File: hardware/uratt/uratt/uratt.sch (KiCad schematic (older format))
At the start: 62 parts

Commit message: more schematic work.. power supply, lip charger, etc
more schematic work.. power supply, lip charger, etc
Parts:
- added C? (x2): .1uF, symbol Device:C_Small
- added C?: 1uF, symbol Device:C_Small
- added C? (x2): 2.2uF, symbol Device:C_Small
- added C? (x2): 4.7uF, symbol Device:C_Small
- added C?: 220uF, symbol Device:CP1_Small
- added C?: 10uF, symbol Device:C_Small
- added D?: LED, symbol Device:LED
- added J?: Conn_01x02, symbol Connector_Generic:Conn_01x02
- added L?: 6.8uH, symbol Device:L
- added R? (x5): 10K, symbol Device:R_Small_US
- added R? (x2): 1K, symbol Device:R_Small_US
- added R?: 270, symbol Device:R_Small_US
- added R?: 2K, symbol Device:R_Small_US
- added R?: 0, symbol Device:R_Small_US
- added R?: R3, symbol Device:R_Small_US
- added R?: R4, symbol Device:R_Small_US
- added R?: R1, symbol Device:R_Small_US
- added R?: R2, symbol Device:R_Small_US
- added U?: MCP73832-2-OT, Package_TO_SOT_SMD:SOT-23-5, symbol Battery_Management:MCP73832-2-OT
- added U?: TPS2115A, symbol uratt:TPS2115A
- added U?: TPS61032PWP, symbol uratt:TPS6103x
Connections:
- net labels added: +5VIN, +VBATT, +VSW, 5V_ENABLE, CHARGE_STATUS, GNDPWR, LOW_BAT, N_PWR_LOSS, SHUTDOWN
- wire segments 236 -> 376
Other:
- note added: "Charge Current Resistor\nI_CHG = 1000 / R_PROG\nR_PROG = 2K : I_CHG = 500mA"
- note added: "D1=0, D0=0, IN2>IN1=X, STAT=HI-Z, OUT=IN2\nD1=0, D0=1, IN2>IN1=N, STAT=0, OUT=IN1\nD1=0, D0=1, IN2>IN1=Y, STAT=HI-Z, OUT=IN2\nD1=1, D0=0, IN2>IN1=X, STAT=0, OUT=IN1\nD1=1, D0=1, IN2>IN1=X, STAT=0, OUT=HI-Z\n\n\n"
- note added: "R_PROG\n"
- moved on the sheet: C?, D?, FB?, J?, R?, U?

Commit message: mostly feature complete schematic?
Split off pages for power and front panel, assign all I/O, add alarm & exp, add 10V option off 5V boost for optional stepper driver (for cabinet lock-bot), ESD protection
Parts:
- removed C?: 10uF, symbol Device:CP1_Small
- removed C? (x2): 0.1uF, symbol Device:C_Small
- removed C? (x2): 1uF, symbol Device:C_Small
- removed C? (x2): .1uF, symbol Device:C_Small
- removed C? (x2): 2.2uF, symbol Device:C_Small
- removed C? (x2): 4.7uF, symbol Device:C_Small
- removed C?: 220uF, symbol Device:CP1_Small
- removed C?: 10uF, symbol Device:C_Small
- removed D?: LED, symbol Device:LED
- removed J? (x2): Conn_01x02, symbol Connector_Generic:Conn_01x02
- removed L?: 6.8uH, symbol Device:L
- removed Q?: DMP31D0U, Package_TO_SOT_SMD:SOT-23, symbol Transistor_FET:BSS83P
- removed R?: 220, symbol Device:R_Small_US
- removed R? (x6): 10K, symbol Device:R_Small_US
- removed R? (x2): 1K, symbol Device:R_Small_US
- removed R?: 270, symbol Device:R_Small_US
- removed R?: 2K, symbol Device:R_Small_US
- removed R?: 0, symbol Device:R_Small_US
- removed R?: R3, symbol Device:R_Small_US
- removed R?: R4, symbol Device:R_Small_US
- removed R?: R1, symbol Device:R_Small_US
- removed R?: R2, symbol Device:R_Small_US
- removed U?: MP6513, Package_TO_SOT_SMD:TSOT-23-6, symbol uratt:MP6513
- removed U?: ER-TFT0.96-1, symbol uratt:ER-TFT0.96-1
- removed U?: AP2112K-3.3, Package_TO_SOT_SMD:SOT-23-5, symbol Regulator_Linear:AP2112K-3.3
- removed U?: MCP73832-2-OT, Package_TO_SOT_SMD:SOT-23-5, symbol Battery_Management:MCP73832-2-OT
- removed U?: TPS2115A, symbol uratt:TPS2115A
- removed U?: TPS61032PWP, symbol uratt:TPS6103x
- added C? (x2): .1uF, symbol Device:C_Small
- added C? (x2): 2.2uF, symbol Device:C_Small
- added D?: DT1240A-08LP3810, Package_DFN_QFN:UDFN-9_1.0x3.8mm_P0.5mm, symbol Power_Protection:DT1240A-08LP3810
- added D? (x2): BAT54S, Package_TO_SOT_SMD:SOT-23, symbol Diode:BAT54S
- added J?: Conn_01x10, symbol Connector_Generic:Conn_01x10
- added J?: Conn_01x04, symbol Connector_Generic:Conn_01x04
- added R? (x5): 47, symbol Device:R_Small_US
- C?: value 100uF/6.3V -> 100uF
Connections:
- net labels added: +3.3VSW, +5VSW, +5VUSB, ALARM_SW, EXP, FP_TOUCH_BTN, PWR_ENABLE
- net labels removed: +5V, +5VIN, +5VP, +VBATT, +VSW, 5V_ENABLE, 5V_RFID_TX, CHARGE_STATUS, GNDPWR, RFID_RX, RFID_TX
- wire segments 376 -> 273
- no-connect marks 13 -> 20
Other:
- note added: "ALARM & EXP I/O"
- note added: "FRONT PANEL CONNECTOR"
- note added: "POPULATE ONLY ONE\n5V is FB?\n3.3V is FB?"
- note removed: "BACKLIGHT\nVF=3.2V IF=15mA\n"
- note removed: "Charge Current Resistor\nI_CHG = 1000 / R_PROG\nR_PROG = 2K : I_CHG = 500mA"
- note removed: "D1=0, D0=0, IN2>IN1=X, STAT=HI-Z, OUT=IN2\nD1=0, D0=1, IN2>IN1=N, STAT=0, OUT=IN1\nD1=0, D0=1, IN2>IN1=Y, STAT=HI-Z, OUT=IN2\nD1=1, D0=0, IN2>IN1=X, STAT=0, OUT=IN1\nD1=1, D0=1, IN2>IN1=X, STAT=0, OUT=HI-Z\n\n\n"
- note removed: "DC MOTOR CONTROL"
- note removed: "GRAPHIC LCD"
- note removed: "POPULATE ONLY ONE\n5V is R?\n3.3V is R?"
- note removed: "RFID_TX is the OUTPUT from the external RFID module (transmitted RFID tag data)\nRFID_RX is the INPUT to the external RFID module (optional command to RFID)"
- note removed: "R_PROG\n"
- moved on the sheet: BZ?, C?, D?, FB?, J?, Q?, R?, U?

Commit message: uRATT rough footprint assignment and placement for fitment
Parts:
- removed BZ?: Buzzer, symbol Device:Buzzer
- removed Q? (x2): S8050, Package_TO_SOT_THT:TO-92_Inline, symbol Transistor_BJT:S8050
- removed Q?: 2N7002, Package_TO_SOT_SMD:SOT-23, symbol Transistor_FET:2N7002
- removed R?: 100, symbol Device:R_Small_US
- removed R?: 1K, symbol Device:R_Small_US
- added Q1, Q2: MMBT3904, Package_TO_SOT_SMD:SOT-23, symbol Transistor_BJT:MMBT3904
- C1, C5: renamed from C?; footprint (none) -> Capacitor_SMD:C_0805_2012Metric
- C10, C11, C13, C14, C15, C16, C2, C3, C4, C6, C7, C8, C9: renamed from C?; footprint (none) -> Capacitor_SMD:C_0603_1608Metric
- C12: renamed from C?; footprint (none) -> Capacitor_SMD:CP_Elec_5x3
- D1: renamed from D?; footprint Diode_THT:D_DO-41_SOD81_P10.16mm_Horizontal -> Diode_SMD:D_0805_2012Metric
- FB1, FB2: renamed from FB?; footprint (none) -> Inductor_SMD:L_0603_1608Metric
- J1: renamed from J?; footprint (none) -> Connector_USB:USB_Micro-B_Molex-105133-0001
- J2: renamed from J?; footprint (none) -> Connector_Card:microSD_HC_Hirose_DM3D-SF
- J3: renamed from J?; footprint (none) -> Connector_PinHeader_2.54mm:PinHeader_1x10_P2.54mm_Vertical
- J4, J5: renamed from J?; footprint (none) -> Connector_JST:JST_PH_B4B-PH-K_1x04_P2.00mm_Vertical
- R1, R10, R11, R12, R13, R14, R15, R16, R17, R19, R2, R21, R22, R23, R24, R25, R26, R27, R3, R4, R5, R6, R7, R8, R9: renamed from R?; footprint (none) -> Resistor_SMD:R_0603_1608Metric
- SW1, SW2: renamed from SW?; footprint (none) -> Button_Switch_SMD:SW_Push_1P1T_NO_CK_KMR2
- gave numbers to parts that had none: 8
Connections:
- net BEEPER: now also D2.9 (K8), J3.8 (Pin_8)
- net DTR: now also Q2.2 (E)
- net EN: now also Q1.3 (C)
- net GND: no longer J3.8 (Pin_8)
- net IO0: now also Q2.3 (C)
- net RTS: now also Q1.2 (E)
- net at R12.1: now also Q1.1 (B)
- net at R13.1: now also Q2.1 (B)
- no-connect marks 20 -> 19
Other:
- note removed: "PIEZO BEEPER"

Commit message: import actual board outline DXF and adjust rough placement
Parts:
- J3: footprint Connector_PinHeader_2.54mm:PinHeader_1x10_P2.54mm_Vertical -> Connector_PinHeader_2.00mm:PinHeader_1x10_P2.00mm_Vertical
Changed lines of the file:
@@
 F 0 "J3" H 14300 2100 50  0000 C CNN
 F 1 "Conn_01x10" H 14450 950 50  0000 C CNN
-F 2 "Connector_PinHeader_2.54mm:PinHeader_1x10_P2.54mm_Vertical" H 14300 1600 50  0001 C CNN
+F 2 "Connector_PinHeader_2.00mm:PinHeader_1x10_P2.00mm_Vertical" H 14300 1600 50  0001 C CNN
 F 3 "~" H 14300 1600 50  0001 C CNN
 	1    14300 1600

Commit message: WIP routing
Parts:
- J1: footprint Connector_USB:USB_Micro-B_Molex-105133-0001 -> Connector_FFC-FPC:TE_1-1734839-0_1x10-1MP_P0.5mm_Horizontal
- J3: footprint Connector_PinHeader_2.00mm:PinHeader_1x10_P2.00mm_Vertical -> Connector_FFC-FPC:Hirose_FH12-10S-0.5SH_1x10-1MP_P0.50mm_Horizontal
- renumbered R19 to R18, R21 to R19, R22 to R20, R23 to R21, R24 to R22, R25 to R23, R26 to R24, R27 to R25
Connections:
- net +3.3VSW: now also C5.1, C6.1, U2.5 (VIO), U2.6 (VDD), U2.7 (REGIN)
- net +3V3: no longer C5.1, C6.1, U2.5 (VIO), U2.6 (VDD), U2.7 (REGIN)
- net BEEPER: now also D2.6 (K5); no longer D2.9 (K8)
- net FP_TOUCH_BTN: now also D2.5 (K4); no longer D2.8 (K7)
- net LCD_CLK: now also D2.7 (K6); no longer D2.6 (K5)
- net LCD_CS: now also D2.9 (K8); no longer D2.2 (K2)
- net LCD_DC: now also D2.8 (K7); no longer D2.5 (K4)
- net LCD_MOSI: now also D2.4 (K3); no longer D2.7 (K6)
- net LCD_RESET: now also D2.2 (K2); no longer D2.4 (K3)

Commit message: fully routed, DRC'd, outlined w/breakaways, pending final review
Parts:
- J1: footprint Connector_FFC-FPC:TE_1-1734839-0_1x10-1MP_P0.5mm_Horizontal -> Connector_USB:USB_Micro-B_Molex-105133-0001
- J3: footprint Connector_FFC-FPC:Hirose_FH12-10S-0.5SH_1x10-1MP_P0.50mm_Horizontal -> Connector_FFC-FPC:TE_1-1734839-0_1x10-1MP_P0.5mm_Horizontal
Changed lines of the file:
@@
 F 0 "J1" H 1357 2017 50  0000 C CNN
 F 1 "USB_B_Micro" H 1357 1926 50  0000 C CNN
-F 2 "Connector_FFC-FPC:TE_1-1734839-0_1x10-1MP_P0.5mm_Horizontal" H 1450 1500 50  0001 C CNN
+F 2 "Connector_USB:USB_Micro-B_Molex-105133-0001" H 1450 1500 50  0001 C CNN
 F 3 "~" H 1450 1500 50  0001 C CNN
 	1    1300 1550
@@
 F 0 "J3" H 14300 2100 50  0000 C CNN
 F 1 "Conn_01x10" H 14450 950 50  0000 C CNN
-F 2 "Connector_FFC-FPC:Hirose_FH12-10S-0.5SH_1x10-1MP_P0.50mm_Horizontal" H 14300 1600 50  0001 C CNN
+F 2 "Connector_FFC-FPC:TE_1-1734839-0_1x10-1MP_P0.5mm_Horizontal" H 14300 1600 50  0001 C CNN
 F 3 "~" H 14300 1600 50  0001 C CNN
 	1    14300 1600
@@
 Connection ~ 4450 1050
 $Comp
-L uratt:+3.3VSW #PWR?
+L uratt:+3.3VSW #PWR0102
 U 1 1 601AE667
 P 3950 2350
-F 0 "#PWR?" H 3950 2200 50  0001 C CNN
+F 0 "#PWR0102" H 3950 2200 50  0001 C CNN
 F 1 "+3.3VSW" H 3965 2523 50  0000 C CNN
 F 2 "" H 3950 2350 50  0001 C CNN

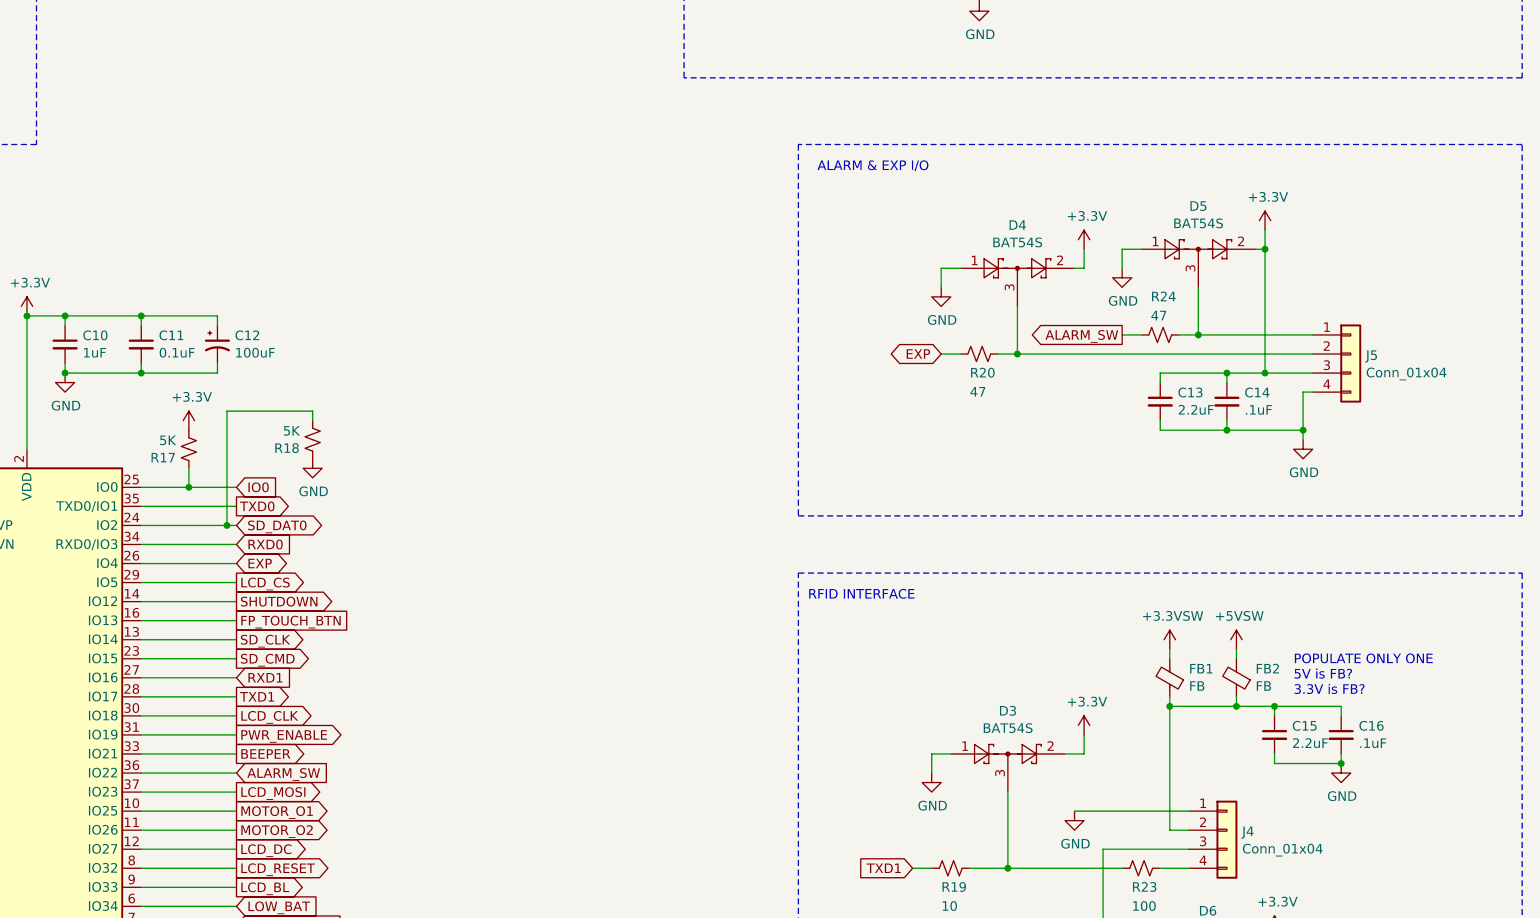
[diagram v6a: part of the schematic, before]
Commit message: add wire passthru slot, move & finalize flat flex, bigger fp button, 10V option for motor, exp connector now Grove with I2C option
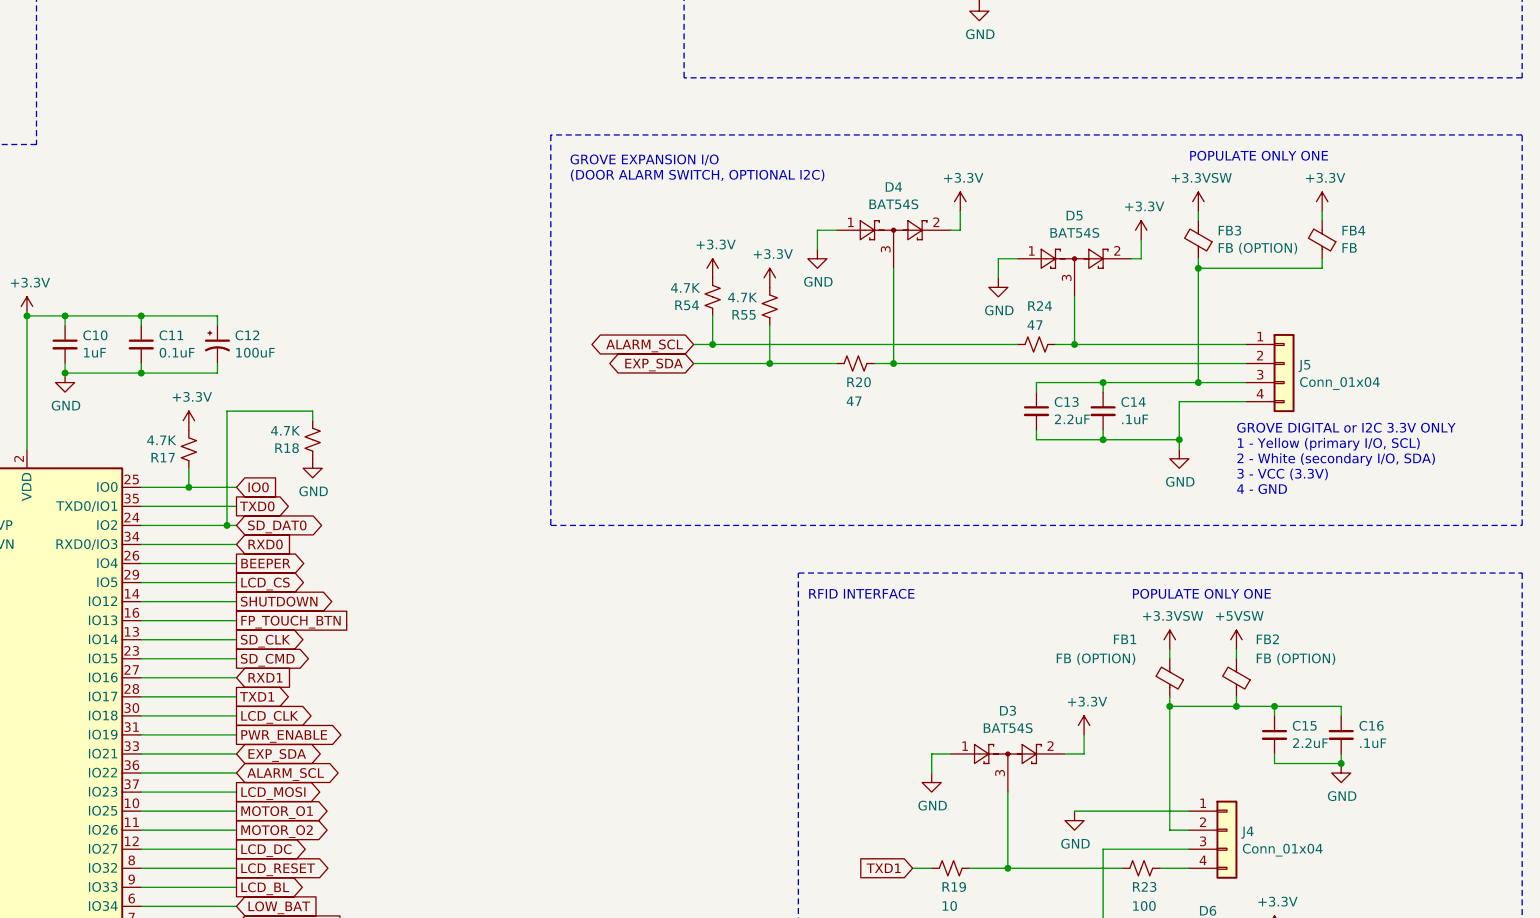
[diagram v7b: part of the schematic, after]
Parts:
- added FB3: FB (OPTION), Inductor_SMD:L_0603_1608Metric, symbol Device:Ferrite_Bead_Small
- added FB4: FB, Inductor_SMD:L_0603_1608Metric, symbol Device:Ferrite_Bead_Small
- added R54, R55: 4.7K, Resistor_SMD:R_0603_1608Metric, symbol Device:R_Small_US
- FB1, FB2: value FB -> FB (OPTION)
- J5: footprint Connector_JST:JST_PH_B4B-PH-K_1x04_P2.00mm_Vertical -> Connector:NS-Tech_Grove_1x04_P2mm_Vertical
- R17, R18: value 5K -> 4.7K
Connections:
- net +3.3VSW: now also FB3.2
- net +3V3: now also FB4.2, R54.2, R55.2; no longer C13.1, C14.1, J5.3 (Pin_3)
- net BEEPER: now also U3.26 (IO4); no longer U3.33 (IO21)
- net ALARM_SW renamed ALARM_SCL
- net ALARM_SCL: now also R54.1
- net EXP renamed EXP_SDA
- net EXP_SDA: now also U3.33 (IO21), R55.1; no longer U3.26 (IO4)
- new net: C13.1, C14.1, FB3.1, FB4.1, J5.3 (Pin_3)
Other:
- note added: "GROVE DIGITAL or I2C 3.3V ONLY\n1 - Yellow (primary I/O, SCL)\n2 - White (secondary I/O, SDA)\n3 - VCC (3.3V)\n4 - GND"
- note added: "GROVE EXPANSION I/O\n(DOOR ALARM SWITCH, OPTIONAL I2C)"
- note added: "POPULATE ONLY ONE"
- note removed: "ALARM & EXP I/O"
- note removed: "POPULATE ONLY ONE\n5V is FB?\n3.3V is FB?"
- moved on the sheet: C13, C14, D4, D5, J5, R20, R24

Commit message: completed BOM, 3D STEP export
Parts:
- C1, C5: Digikey (none) -> 1276-1096-1-ND
- C10, C3: Digikey (none) -> 587-2834-1-ND
- C11, C4: Digikey (none) -> 732-7939-1-ND
- C12: Digikey (none) -> PCE4156CT-ND
- C13, C15: Digikey (none) -> 1276-1085-1-ND
- C14, C16, C2, C6, C7, C8, C9: value .1uF -> 0.1uF; Digikey (none) -> 732-7939-1-ND
- D1: value 1N5819 -> SD0805S020S1R0; Digikey (none) -> 478-7800-1-ND
- D2: value DT1240A-08LP3810 -> DT1240A-08LP3810-7; Digikey (none) -> DT1240A-08LP3810-7DICT-ND
- D3, D4, D5, D6: Digikey (none) -> BAT54SLT1GOSCT-ND
- FB1, FB2, FB3: Digikey (none) -> 490-1012-1-ND
- FB4: value FB -> FB (OPTION); Digikey (none) -> 490-1012-1-ND
- J1: Digikey (none) -> WM9734CT-ND
- J2: Digikey (none) -> HR1941CT-ND
- J3: Alt MFR Part (none) -> ZF5S-10-01-T-WT-TR; Digikey (none) -> A100293CT-ND
- J4: Digikey (none) -> 455-1706-ND
- J5: Digikey (none) -> 1597-1082-ND
- Q1, Q2: Digikey (none) -> MMBT3904LT1GOSCT-ND
- R1, R2, R20, R24, R3: Digikey (none) -> 13-RT0603FRE0747RLCT-ND
- R10, R14, R15: Digikey (none) -> YAG5742CT-ND
- R11: Digikey (none) -> 2019-RK73Z1JTTDCT-ND
- R12, R13, R16: Digikey (none) -> YAG3353CT-ND
- R17, R18, R54, R55: Digikey (none) -> YAG1238CT-ND
- R19, R25: Digikey (none) -> 13-RE0603FRE0710RLCT-ND
- R21: Digikey (none) -> 13-RE0603FRE071KLCT-ND
- R22: Digikey (none) -> 13-RT0603FRE072K05LCT-ND
- R23: Digikey (none) -> 13-RE0603FRE07100RLCT-ND
- R4: Digikey (none) -> YAG5727CT-ND
- R5, R6, R7, R8, R9: Digikey (none) -> YAG2321CT-ND
- SW1, SW2: Digikey (none) -> CKN10247CT-ND
- U1: value SN65220 -> SN65220DBVR; Digikey (none) -> 296-9694-1-ND
- U2: value CP2102N-A01-GQFN24 -> CP2102N-A02-GQFN24; Digikey (none) -> 336-5887-ND
- U3: value ESP32-WROOM-32 -> ESP32-WROOM-32E; Digikey (none) -> 1965-ESP32-WROOM-32E(16MB)CT-ND
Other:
- note added: "CONNECT J3 TO FRONT PANEL BOARD\n10POS 0.50MM FFC TOP/BOTTOM STYLE\n\nSAMTEC P/N FJH-10-R-02.00-4\nhttp://suddendocs.samtec.com/catalog_english/fjh.pdf"
